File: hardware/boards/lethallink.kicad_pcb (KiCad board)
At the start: 6 copper layers, 86 x 111.1 mm, 2 parts, among them J1 PCIe-x4

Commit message: Imported the parts onto the board, and group things roughly by functional group in preperation to route
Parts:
- removed G***: LOGO, lethalbit-graphics:Antifaschistische Aktion_600dpi
- added C1: 10uF, Capacitor_SMD:C_1206_3216Metric, F.Cu at (243.3, 144.5)
- added C10: 10pF, Capacitor_SMD:C_0603_1608Metric, F.Cu at (271.4, 134.2)
- added C11: 470pF, Capacitor_SMD:C_0603_1608Metric, F.Cu at (267.0, 136.7)
- added C12: 1uF, Capacitor_SMD:C_0603_1608Metric, F.Cu at (251.0, 154.0)
- added C13: 0.1uF, Capacitor_SMD:C_0603_1608Metric, F.Cu at (256.2, 146.9)
- added C14: 22uF, Capacitor_SMD:C_1206_3216Metric, F.Cu at (237.7, 141.2)
- added C15: 0.1uF, Capacitor_SMD:C_0603_1608Metric, F.Cu at (261.8, 141.7)
- added C16: 0.1uF, Capacitor_SMD:C_0603_1608Metric, F.Cu at (252.2, 151.3)
- added C17: 2.2nF, Capacitor_SMD:C_0603_1608Metric, F.Cu at (271.5, 131.6)
- added C18: 10pF, Capacitor_SMD:C_0603_1608Metric, F.Cu at (247.0, 154.0)
- added C19: 1.8nF, Capacitor_SMD:C_0603_1608Metric, F.Cu at (262.6, 138.7)
- added C2: 10uF, Capacitor_SMD:C_1206_3216Metric, F.Cu at (243.3, 141.2)
- added C20: 10pF, Capacitor_SMD:C_0603_1608Metric, F.Cu at (252.2, 148.8)
- added C21: 22uF, Capacitor_SMD:C_1206_3216Metric, F.Cu at (252.6, 132.0)
- added C22: 22uF, Capacitor_SMD:C_1206_3216Metric, F.Cu at (237.7, 147.8)
- added C23: 10nF, Capacitor_SMD:C_0402_1005Metric, F.Cu at (40.9, -24.9)
- added C24: 10nF, Capacitor_SMD:C_0402_1005Metric, F.Cu at (32.2, -28.9)
- added C25: 10nF, Capacitor_SMD:C_0402_1005Metric, F.Cu at (32.2, -26.9)
- added C26: 10nF, Capacitor_SMD:C_0402_1005Metric, F.Cu at (38.0, -22.9)
- added C27: 10nF, Capacitor_SMD:C_0402_1005Metric, F.Cu at (43.9, -28.9)
- added C28: 100nF, Capacitor_SMD:C_0402_1005Metric, F.Cu at (40.9, -26.9)
- added C29: 100nF, Capacitor_SMD:C_0402_1005Metric, F.Cu at (38.0, -24.9)
- added C3: 1uF, Capacitor_SMD:C_0603_1608Metric, F.Cu at (266.6, 139.2)
- added C30: 100nF, Capacitor_SMD:C_0402_1005Metric, F.Cu at (35.1, -22.9)
- added C31: 100nF, Capacitor_SMD:C_0402_1005Metric, F.Cu at (40.9, -28.9)
- added C32: 100nF, Capacitor_SMD:C_0402_1005Metric, F.Cu at (38.0, -26.9)
- added C33: 10nF, Capacitor_SMD:C_0402_1005Metric, F.Cu at (35.1, -24.9)
- added C34: 100nF, Capacitor_SMD:C_0402_1005Metric, F.Cu at (32.2, -22.9)
- added C35: 1nF, Capacitor_SMD:C_0402_1005Metric, F.Cu at (38.0, -28.9)
- added C36: 100nF, Capacitor_SMD:C_0402_1005Metric, F.Cu at (35.1, -26.9)
- added C37: 10nF, Capacitor_SMD:C_0402_1005Metric, F.Cu at (32.2, -24.9)
- added C38: 1nF, Capacitor_SMD:C_0402_1005Metric, F.Cu at (35.1, -28.9)
- added C39: 0.1uF, Capacitor_SMD:C_0603_1608Metric, F.Cu at (19.4, -41.2)
- added C4: 10uF, Capacitor_SMD:C_1206_3216Metric, F.Cu at (237.7, 144.5)
- added C5: 10uF, Capacitor_SMD:C_1206_3216Metric, F.Cu at (247.0, 132.0)
- added C6: 10pF, Capacitor_SMD:C_0603_1608Metric, F.Cu at (275.5, 131.6)
- added C7: 330pF, Capacitor_SMD:C_0603_1608Metric, F.Cu at (261.4, 144.3)
- added C8: 0.1uF, Capacitor_SMD:C_0603_1608Metric, F.Cu at (256.2, 149.4)
- added C9: 22uF, Capacitor_SMD:C_1206_3216Metric, F.Cu at (247.0, 135.2)
- added D1: GRN, LED_SMD:LED_0603_1608Metric, F.Cu at (263.0, 136.2)
- added D2: GRN, LED_SMD:LED_0603_1608Metric, F.Cu at (253.4, 144.3)
- added D3: GRN, LED_SMD:LED_0603_1608Metric, F.Cu at (267.5, 131.6)
- added D4: GRN, LED_SMD:LED_0603_1608Metric, F.Cu at (248.2, 151.5)
- added D5: GRN, LED_SMD:LED_0603_1608Metric, F.Cu at (257.8, 141.7)
- added D6: GRN, LED_SMD:LED_0603_1608Metric, F.Cu at (248.2, 148.9)
- added D7: GRN, LED_SMD:LED_0603_1608Metric, F.Cu at (253.8, 141.7)
- added FB1: 100 @ 100MHz, Resistor_SMD:R_0603_1608Metric, F.Cu at (61.2, 142.8)
- added FB2: 220 @ 100Mhz, Resistor_SMD:R_0603_1608Metric, F.Cu at (61.2, 145.3)
- added FB3: 220 @ 100Mhz, Resistor_SMD:R_0603_1608Metric, F.Cu at (65.2, 142.8)
- added G1: Antifaschistische_Aktion, lethalbit-graphics:Antifaschistische Aktion_100dpi, F.Cu at (178.3, 22.2)
- added J2: USB3_Micro_B_Amphenol, lethalbit:USB3_Micro_B_Amphenol, F.Cu at (19.1, 60.5)
- added L1: 8.2uH, lethalbit:L_Coilcraft_XxL4040, F.Cu at (243.3, 148.9)
- added L2: 6.8uH, lethalbit:L_Coilcraft_XxL4030, F.Cu at (258.2, 133.1)
- added L3: 3.3uH, lethalbit:L_Coilcraft_XxL4020, F.Cu at (237.7, 152.2)
- added L4: 4.7uH, lethalbit:L_Coilcraft_XxL4020, F.Cu at (248.9, 139.7)
- added Q1: Q_NMOS_GSD, Package_TO_SOT_SMD:SOT-23, F.Cu at (258.4, 138.2)
- added Q2: Q_NMOS_GSD, Package_TO_SOT_SMD:SOT-23, F.Cu at (242.7, 154.0)
- added Q3: Q_NMOS_GSD, Package_TO_SOT_SMD:SOT-23, F.Cu at (263.2, 132.6)
- added Q4: Q_NMOS_GSD, Package_TO_SOT_SMD:SOT-23, F.Cu at (253.9, 138.2)
- added Q5: SI7232DN-T1-GE3, lethalbit:Si7232DN, F.Cu at (248.8, 145.0)
- added R1: 20, Resistor_SMD:R_0603_1608Metric, F.Cu at (259.0, 151.9)
- added R10: 10k, Resistor_SMD:R_0603_1608Metric, F.Cu at (271.0, 136.7)
- added R11: 12k1, Resistor_SMD:R_0603_1608Metric, F.Cu at (255.0, 153.9)
- added R12: 15k, Resistor_SMD:R_0603_1608Metric, F.Cu at (277.9, 141.7)
- added R13: 10K, Resistor_SMD:R_0603_1608Metric, F.Cu at (278.7, 139.1)
- added R14: 12k1, Resistor_SMD:R_0603_1608Metric, F.Cu at (265.8, 141.7)
- added R15: 10k, Resistor_SMD:R_0603_1608Metric, F.Cu at (257.4, 144.3)
- added R16: 8k2, Resistor_SMD:R_0603_1608Metric, F.Cu at (274.7, 139.2)
- added R17: 127k, Resistor_SMD:R_0603_1608Metric, F.Cu at (276.2, 146.7)
- added R18: 4k99, Resistor_SMD:R_0603_1608Metric, F.Cu at (277.4, 144.2)
- added R19: 10k, Resistor_SMD:R_0603_1608Metric, F.Cu at (272.2, 149.2)
- added R2: 20, Resistor_SMD:R_0603_1608Metric, F.Cu at (269.9, 141.7)
- added R20: 10k, Resistor_SMD:R_0603_1608Metric, F.Cu at (267.0, 154.3)
- added R21: 4k99, Resistor_SMD:R_0603_1608Metric, F.Cu at (267.4, 134.2)
- added R22: 8k2, Resistor_SMD:R_0603_1608Metric, F.Cu at (267.0, 151.8)
- added R23: 10K, Resistor_SMD:R_0603_1608Metric, F.Cu at (272.2, 146.7)
- added R24: 10K, Resistor_SMD:R_0603_1608Metric, F.Cu at (275.4, 136.6)
- added R25: 3k3, Resistor_SMD:R_0603_1608Metric, F.Cu at (273.4, 144.2)
- added R26: 4k22, Resistor_SMD:R_0603_1608Metric, F.Cu at (268.2, 149.2)
- added R27: 10k, Resistor_SMD:R_0603_1608Metric, F.Cu at (263.0, 154.3)
- added R28: 10k, Resistor_SMD:R_0603_1608Metric, F.Cu at (273.9, 141.7)
- added R29: 10k, Resistor_SMD:R_0603_1608Metric, F.Cu at (263.0, 151.8)
- added R3: 1k74, Resistor_SMD:R_0603_1608Metric, F.Cu at (264.2, 146.8)
- added R30: 10k, Resistor_SMD:R_0603_1608Metric, F.Cu at (268.2, 146.7)
- added R31: 20, Resistor_SMD:R_0603_1608Metric, F.Cu at (260.2, 146.8)
- added R32: 20, Resistor_SMD:R_0603_1608Metric, F.Cu at (269.4, 144.2)
- added R33: 20, Resistor_SMD:R_0603_1608Metric, F.Cu at (264.2, 149.3)
- added R34: 20, Resistor_SMD:R_0603_1608Metric, F.Cu at (259.0, 154.4)
- added R35: 1M, Resistor_SMD:R_0603_1608Metric, F.Cu at (19.4, -35.7)
- added R4: 24k9, Resistor_SMD:R_0603_1608Metric, F.Cu at (270.6, 139.2)
- added R5: 21k, Resistor_SMD:R_0603_1608Metric, F.Cu at (265.4, 144.2)
- added R6: 10K, Resistor_SMD:R_0603_1608Metric, F.Cu at (260.2, 149.3)
- added R7: 21k1, Resistor_SMD:R_0603_1608Metric, F.Cu at (275.4, 134.1)
- added U1: ECP5UM5G-381caBGA, lethalbit:318caBGA, F.Cu at (-22.7, -10.1)
- added U2: ADP5050ACPZ-R7, lethalbit:QFN-48_EP_7x7_Pitch0.5mm, F.Cu at (239.6, 134.9)
- added U3: CYUSB3014, lethalbit:BGA-121_11x11_10.0x10.0mm, F.Cu at (38.3, -42.7)
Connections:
- net +12V renamed Net-(FB1-Pad1)
- net +3V3 renamed Net-(FB2-Pad2)
- net Net-(J1-PadA11) renamed /AUX Control/PERST#
- net Net-(J1-PadA13) renamed /PCIe Interface/REFCLK_P
- net Net-(J1-PadA14) renamed /PCIe Interface/REFCLK_N
- net Net-(J1-PadA16) renamed /PCIe Interface/RX0_P
- net Net-(J1-PadA17) renamed /PCIe Interface/RX0_N
- net Net-(J1-PadA22) renamed /PCIe Interface/RX1_P
- net Net-(J1-PadA23) renamed /PCIe Interface/RX1_N
- net Net-(J1-PadA26) renamed /PCIe Interface/RX2_P
- net Net-(J1-PadA27) renamed /PCIe Interface/RX2_N
- net Net-(J1-PadA30) renamed /PCIe Interface/RX3_P
- net Net-(J1-PadA31) renamed /PCIe Interface/RX3_N
- net Net-(J1-PadA5) renamed /AUX Control/PCIe_TCK
- net Net-(J1-PadA6) renamed /AUX Control/PCIe_TDI
- net Net-(J1-PadA7) renamed /AUX Control/PCIe_TDO
- net Net-(J1-PadA8) renamed /AUX Control/PCIe_TMS
- net Net-(J1-PadB11) renamed /AUX Control/WAKE#
- net Net-(J1-PadB12) renamed /AUX Control/CLKREQ#
- net Net-(J1-PadB14) renamed /PCIe Interface/TX0_P
- net Net-(J1-PadB15) renamed /PCIe Interface/TX0_N
- net Net-(J1-PadB19) renamed /PCIe Interface/TX1_P
- net Net-(J1-PadB20) renamed /PCIe Interface/TX1_N
- net Net-(J1-PadB23) renamed /PCIe Interface/TX2_P
- net Net-(J1-PadB24) renamed /PCIe Interface/TX2_N
- net Net-(J1-PadB27) renamed /PCIe Interface/TX3_P
- net Net-(J1-PadB28) renamed /PCIe Interface/TX3_N
- net Net-(J1-PadB5) renamed /AUX Control/PCIe_SMCLK
- net Net-(J1-PadB6) renamed /AUX Control/PCIe_SMDAT
- net Net-(J1-PadB9) renamed /AUX Control/PCIe_TRST#
- J1 pad B10: +3.3VA -> Net-(FB3-Pad2)

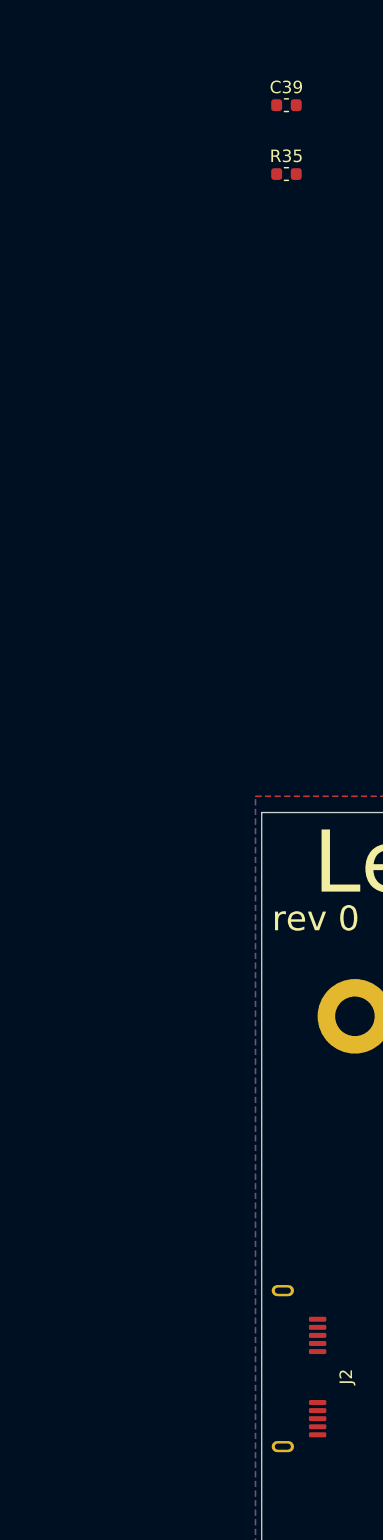
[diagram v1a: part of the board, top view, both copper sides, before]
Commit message: Upped the schematic frame size from A4 to A3 to allow for some more breathing room, it was getting stuff in the powersupply schematic
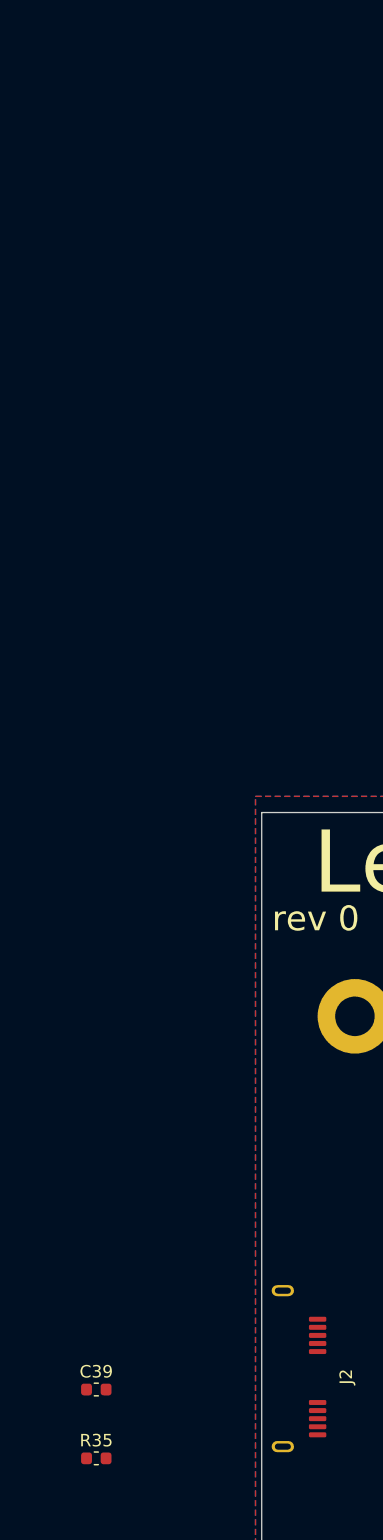
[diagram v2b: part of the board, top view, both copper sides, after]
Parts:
- moved C39 104.5 mm to (4.14, 62.1)
- moved R35 104.5 mm to (4.14, 67.7)
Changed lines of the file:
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@@
   )
   (module Resistor_SMD:R_0603_1608Metric (layer F.Cu)
-    (at 19.44 -35.68)
+    (at 4.14 67.67)
     (descr "Resistor SMD 0603 (1608 Metric), square (rectangular) end terminal, IPC_7351 nominal, (Body size source: http://www.tortai-tech.com/upload/download/2011102023233369053.pdf), generated with kicad-footprint-generator")
     (tags resistor)
@@
   )
   (module Capacitor_SMD:C_0603_1608Metric (layer F.Cu)
-    (at 19.44 -41.22)
+    (at 4.14 62.13)
     (descr "Capacitor SMD 0603 (1608 Metric), square (rectangular) end terminal, IPC_7351 nominal, (Body size source: http://www.tortai-tech.com/upload/download/2011102023233369053.pdf), generated with kicad-footprint-generator")
     (tags capacitor)

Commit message: Pulled the schematic updates into the PCB
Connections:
- C1 pad 2: +12V -> /Power Supply/_12v0
- C2 pad 2: +12V -> /Power Supply/_12v0
- C4 pad 2: +12V -> /Power Supply/_12v0
- C5 pad 2: +12V -> /Power Supply/_12v0
- R17 pad 1: +12V -> /Power Supply/_12v0
- U2 pad 24: +12V -> /Power Supply/_12v0
- U2 pad 25: +12V -> /Power Supply/_12v0
- U2 pad 35: +12V -> /Power Supply/_12v0
- U2 pad 36: +12V -> /Power Supply/_12v0
- U2 pad 4: +12V -> /Power Supply/_12v0
- U2 pad 9: +12V -> /Power Supply/_12v0
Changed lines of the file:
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@@
     (zones 0)
     (modules 97)
-    (nets 450)
+    (nets 451)
   )
   (page A3)
@@
   (net 448 "Net-(U3-PadC1)")
   (net 449 "Net-(U3-PadB1)")
+  (net 450 "/Power Supply/_12v0")
   (net_class Default "This is the default net class."
     (clearance 0.2)
@@
     (add_net "/PCIe Interface/TX3_P")
     (add_net /PRSNT#)
+    (add_net "/Power Supply/_12v0")
     (add_net GND)
     (add_net "Net-(C10-Pad1)")
@@
       (net 93 "Net-(R17-Pad2)"))
     (pad 36 smd rect (at 3.45 -2.75 90) (size 0.25 0.7) (layers F.Cu F.Paste F.Mask)
-      (net 8 +12V))
+      (net 450 "/Power Supply/_12v0"))
     (pad 35 smd rect (at 3.45 -2.25 90) (size 0.25 0.7) (layers F.Cu F.Paste F.Mask)
-      (net 8 +12V))
+      (net 450 "/Power Supply/_12v0"))
     (pad 34 smd rect (at 3.45 -1.75 90) (size 0.25 0.7) (layers F.Cu F.Paste F.Mask)
       (net 21 "Net-(C15-Pad2)"))
@@
       (net 23 "Net-(C16-Pad2)"))
     (pad 25 smd rect (at 3.45 2.75 90) (size 0.25 0.7) (layers F.Cu F.Paste F.Mask)
-      (net 8 +12V))
+      (net 450 "/Power Supply/_12v0"))
     (pad 24 smd rect (at 2.75 3.45) (size 0.25 0.7) (layers F.Cu F.Paste F.Mask)
-      (net 8 +12V))
+      (net 450 "/Power Supply/_12v0"))
     (pad 23 smd rect (at 2.25 3.45) (size 0.25 0.7) (layers F.Cu F.Paste F.Mask)
       (net 94 "Net-(R18-Pad2)"))
@@
       (net 13 "Net-(C8-Pad1)"))
     (pad 9 smd rect (at -3.45 1.25 90) (size 0.25 0.7) (layers F.Cu F.Paste F.Mask)
-      (net 8 +12V))
+      (net 450 "/Power Supply/_12v0"))
     (pad 8 smd rect (at -3.45 0.75 90) (size 0.25 0.7) (layers F.Cu F.Paste F.Mask)
       (net 358 "Net-(U2-Pad8)"))
@@
       (net 5 GND))
     (pad 4 smd rect (at -3.45 -1.25 90) (size 0.25 0.7) (layers F.Cu F.Paste F.Mask)
-      (net 8 +12V))
+      (net 450 "/Power Supply/_12v0"))
     (pad 3 smd rect (at -3.45 -1.75 90) (size 0.25 0.7) (layers F.Cu F.Paste F.Mask)
       (net 19 "Net-(C13-Pad1)"))
@@
       (net 93 "Net-(R17-Pad2)"))
     (pad 1 smd roundrect (at -0.7875 0) (size 0.875 0.95) (layers F.Cu F.Paste F.Mask) (roundrect_rratio 0.25)
-      (net 8 +12V))
+      (net 450 "/Power Supply/_12v0"))
     (model ${KISYS3DMOD}/Resistor_SMD.3dshapes/R_0603_1608Metric.wrl
       (at (xyz 0 0 0))
@@
     (fp_line (start 2.28 1.12) (end -2.28 1.12) (layer F.CrtYd) (width 0.05))
     (pad 2 smd roundrect (at 1.4 0) (size 1.25 1.75) (layers F.Cu F.Paste F.Mask) (roundrect_rratio 0.2)
-      (net 8 +12V))
+      (net 450 "/Power Supply/_12v0"))
     (pad 1 smd roundrect (at -1.4 0) (size 1.25 1.75) (layers F.Cu F.Paste F.Mask) (roundrect_rratio 0.2)
       (net 5 GND))
@@
     (fp_line (start 2.28 1.12) (end -2.28 1.12) (layer F.CrtYd) (width 0.05))
     (pad 2 smd roundrect (at 1.4 0) (size 1.25 1.75) (layers F.Cu F.Paste F.Mask) (roundrect_rratio 0.2)
-      (net 8 +12V))
+      (net 450 "/Power Supply/_12v0"))
     (pad 1 smd roundrect (at -1.4 0) (size 1.25 1.75) (layers F.Cu F.Paste F.Mask) (roundrect_rratio 0.2)
       (net 5 GND))
@@
     (fp_line (start 2.28 1.12) (end -2.28 1.12) (layer F.CrtYd) (width 0.05))
     (pad 2 smd roundrect (at 1.4 0) (size 1.25 1.75) (layers F.Cu F.Paste F.Mask) (roundrect_rratio 0.2)
-      (net 8 +12V))
+      (net 450 "/Power Supply/_12v0"))
     (pad 1 smd roundrect (at -1.4 0) (size 1.25 1.75) (layers F.Cu F.Paste F.Mask) (roundrect_rratio 0.2)
       (net 5 GND))
@@
     (fp_line (start 2.28 1.12) (end -2.28 1.12) (layer F.CrtYd) (width 0.05))
     (pad 2 smd roundrect (at 1.4 0) (size 1.25 1.75) (layers F.Cu F.Paste F.Mask) (roundrect_rratio 0.2)
-      (net 8 +12V))
+      (net 450 "/Power Supply/_12v0"))
     (pad 1 smd roundrect (at -1.4 0) (size 1.25 1.75) (layers F.Cu F.Paste F.Mask) (roundrect_rratio 0.2)
       (net 5 GND))

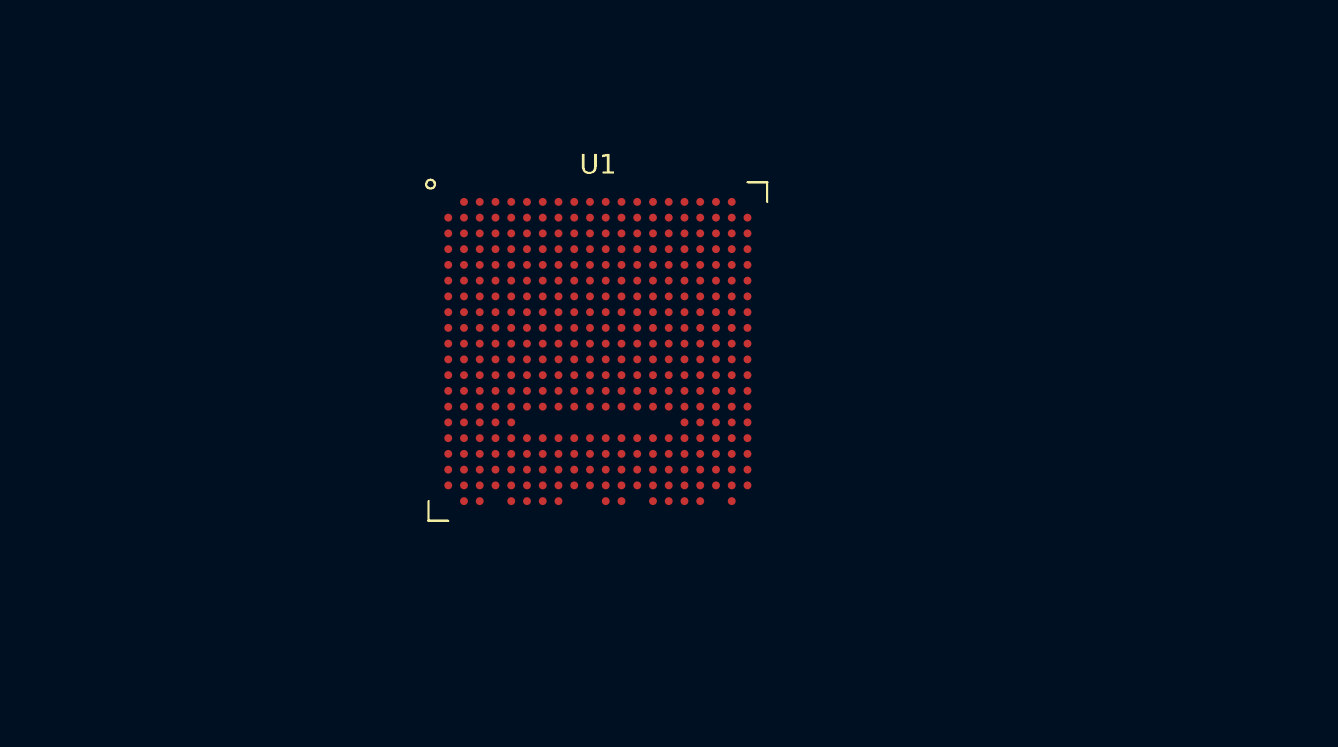
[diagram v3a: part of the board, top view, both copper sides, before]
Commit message: Updated the schematics and PCB to bring the initial bootup config DIP switch for the FPGA into it and also ensured that the FPGA had VCCIO8 tied to 3v3 for proper config voltages
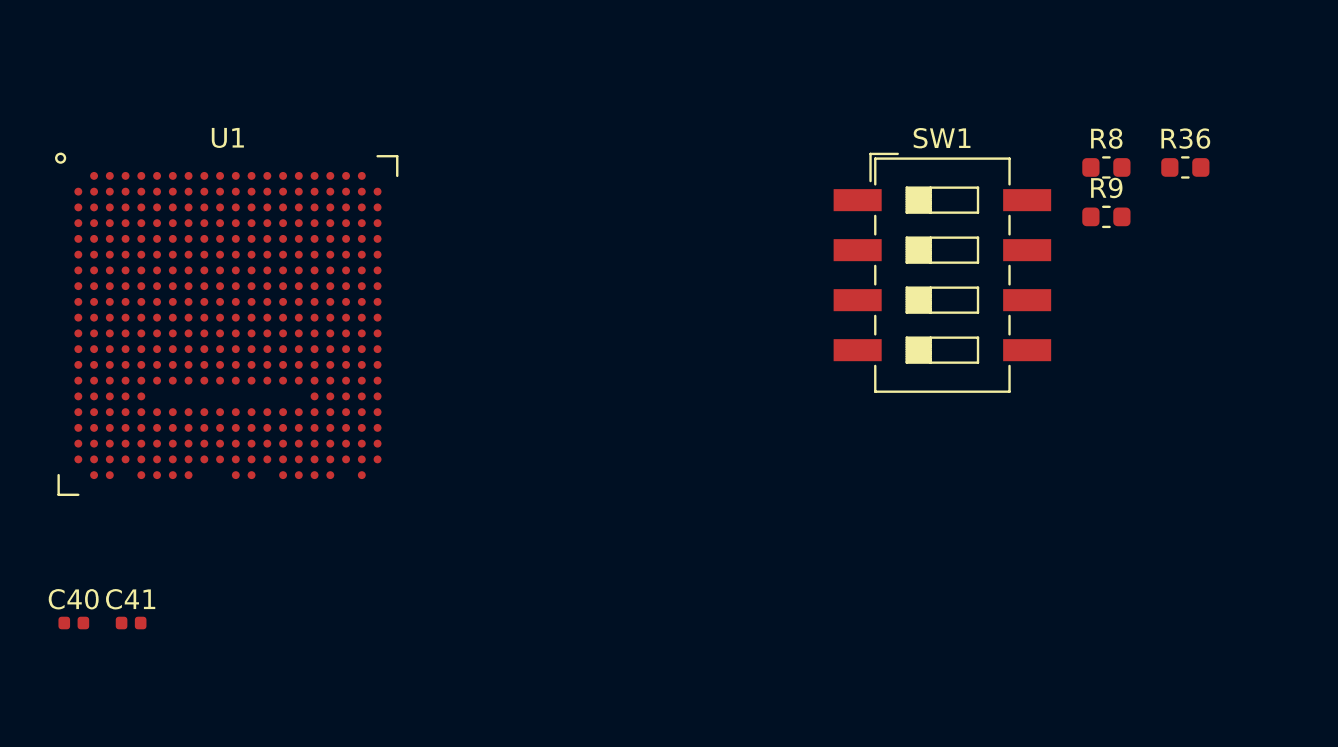
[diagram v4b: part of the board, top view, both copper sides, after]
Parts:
- added C40: 10nF, Capacitor_SMD:C_0402_1005Metric, F.Cu at (-49.3, 3.70)
- added C41: 100nF, Capacitor_SMD:C_0402_1005Metric, F.Cu at (-46.4, 3.70)
- added R36: 1k, Resistor_SMD:R_0603_1608Metric, F.Cu at (7.16, -19.4)
- added R8: 1k, Resistor_SMD:R_0603_1608Metric, F.Cu at (3.15, -19.4)
- added R9: 1k, Resistor_SMD:R_0603_1608Metric, F.Cu at (3.15, -16.9)
- added SW1: SW_DIP_x03, Button_Switch_SMD:SW_DIP_SPSTx04_Slide_6.7x11.72mm_W8.61mm_P2.54mm_LowProfile, F.Cu at (-5.18, -14.0)
- moved U1 18.8 mm to (-41.5, -11.4)
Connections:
- C1 pad 2: /Power Supply/_12v0 -> +12V
- C2 pad 2: /Power Supply/_12v0 -> +12V
- C4 pad 2: /Power Supply/_12v0 -> +12V
- C5 pad 2: /Power Supply/_12v0 -> +12V
- R17 pad 1: /Power Supply/_12v0 -> +12V
- U1 pad P10: Net-(U1-PadP10) -> +3V3
- U1 pad P9: Net-(U1-PadP10) -> +3V3
- U2 pad 24: /Power Supply/_12v0 -> +12V
- U2 pad 25: /Power Supply/_12v0 -> +12V
- U2 pad 35: /Power Supply/_12v0 -> +12V
- U2 pad 36: /Power Supply/_12v0 -> +12V
- U2 pad 4: /Power Supply/_12v0 -> +12V
- U2 pad 9: /Power Supply/_12v0 -> +12V

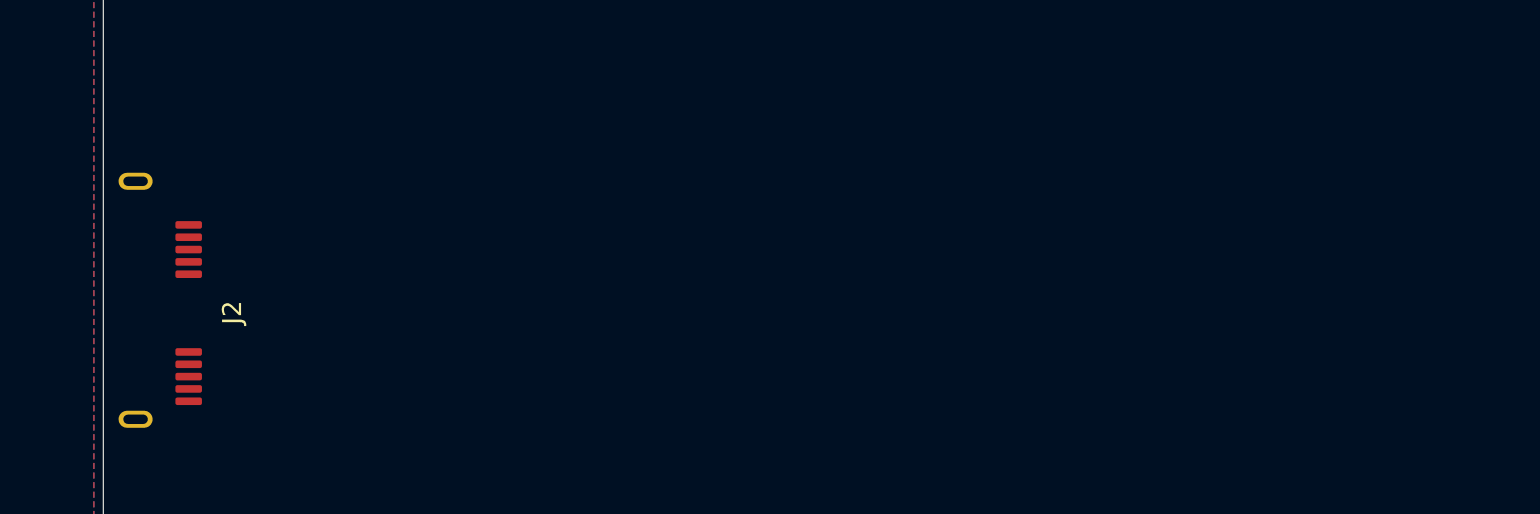
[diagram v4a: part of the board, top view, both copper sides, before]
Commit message: Added the DDR3 Module
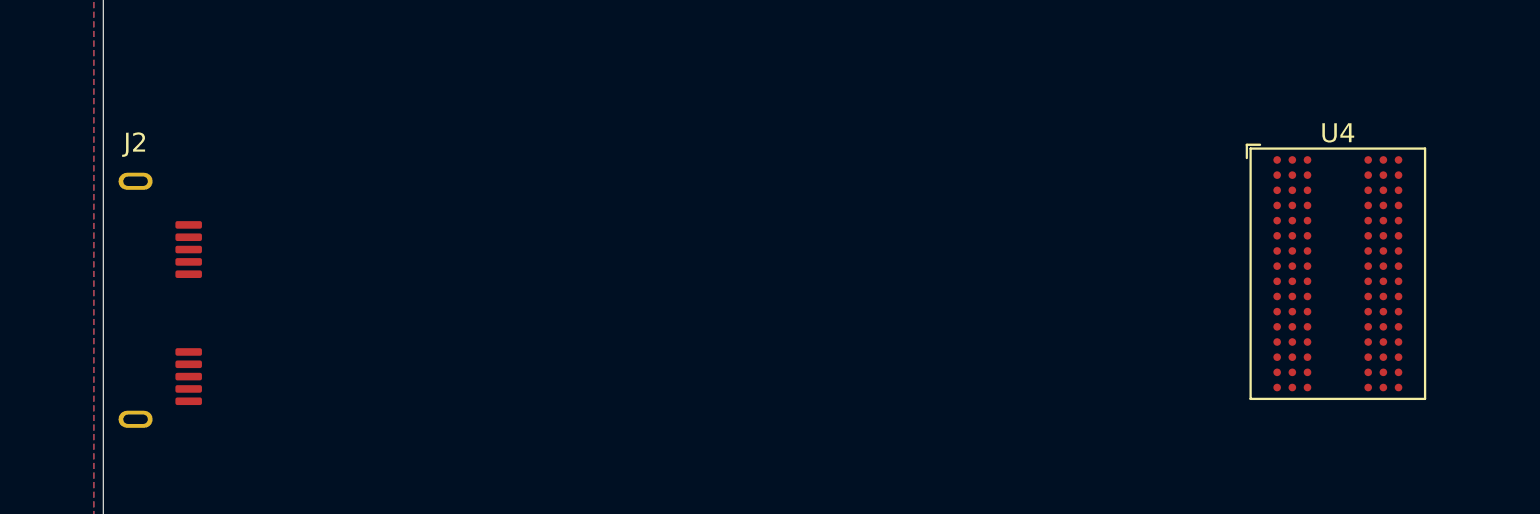
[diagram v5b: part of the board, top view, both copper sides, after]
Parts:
- added U4: IS43TR16256B-125KBL, Package_BGA:BGA-96_9.0x13.0mm_Layout2x3x16_P0.8mm, F.Cu at (82.5, 59.0)
